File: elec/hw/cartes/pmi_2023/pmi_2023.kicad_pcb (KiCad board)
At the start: 2 copper layers, 149.5 x 73 mm, 298 parts, among them J1 con_servo, J10 Conn_01x01_Pin, J11 Conn_01x01_Socket, J12 Conn_01x01_Pin, J13 Conn_01x01_Pin, J14 Conn_01x01_Socket, J15 Conn_01x01_Socket, J16 Conn_01x01_Pin, J17 Conn_01x01_Pin, J19 Conn_01x01_Pin, J2 con_servo, J20 Conn_01x01_Socket, J21 Conn_01x01_Socket, J22 Conn_01x01_Socket, J23 Conn_01x01_Pin, J24 Conn_01x01_Pin, J27 Conn_01x01_Socket, J28 Conn_01x01_Socket, J29 Conn_01x01_Socket, J3 con_servo, J30 Conn_01x01_Socket, J31 Conn_01x01_Pin, J33 Conn_01x01_Socket, J34 Conn_01x01_Socket, J35 Conn_01x01_Pin, J36 Conn_01x01_Socket, J37 Conn_01x01_Pin, J38 Conn_01x01_Socket, J4 con_servo, J41 Conn_01x01_Socket, J42 Conn_01x01_Socket, J43 Conn_01x01_Socket, J44 Conn_01x01_Pin, J45 Conn_01x01_Socket, J46 Conn_01x01_Pin, J5 254, J7 USB4105-GF-A-060, J8 254, J9 Conn_01x01_Socket, Q2 2N7002, Q3 DMP2008UFG-7, SW1 ESE22MH22, SW2 ESE22MH24, SW3 MSS12C02LS-BB2.0, SW4 2425755-1, SW5 DS1040-04RN, SW7 MSS12C02LS-BB2.0, SW8 MSS12C02LS-BB2.0, U1 DRV8231ADDAR, U10 tof_sensor_master, U11 XRA1200PIG16TR-F, U12 LSM6DSO32XTR, U13 GP2S60B, U14 GP2S60B, U15 GP2S60B, U16 GP2S60B, U18 EESX1321, U19 GP2S60B, U2 DRV8231ADDAR, U20 GP2S60B, U22 VL53L5CXV0GC, U23 PCA9685PW, U24 SN74LVC1T45DBV, U25 SN74LVC1T45DBV, U26 SN74LVC1T45DBV, U27 SN74LVC1T45DBV, U28 TLV61070A, U29 TLV61070A, U3 EESX1321, U30 VL53L5CXV0GC, U32 ESP32-S3-WROOM-1, U33 TLV61070A, U34 TLV61070A, U35 LDL1117S33R, U4 EESX1321, U5 AD8531ARTZ, U6 tof_sensor_master, U7 XRA1200PIG16TR-F, U8 GP2S60B, U9 GP2S60B

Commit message: corrected librariesand ongoing routing
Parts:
- moved R32 52.5 mm to (182.6, 141.5)
- moved R33 52.5 mm to (182.6, 140.0)
- moved R44 10.1 mm to (199.7, 137.3), turned to 0 degrees
- moved R80 0.55 mm to (223.3, 115.8)
- moved R81 0.55 mm to (225.8, 115.8)
- turned R119 to 0 degrees
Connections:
- C28 pad 2: GND -> GND_M
- J6 pad 5: (no net) -> /boards interface/com/esp32_dbg_tx_3v3
- R102 pad 2: GND -> GND_M
- R109 pad 2: GND -> GND_M
- R120 pad 2: GND -> GND_M
- R121 pad 2: GND -> GND_M
- R122 pad 2: GND -> GND_M
- R80 pad 2: /boards interface/interface/esp32_scl_3v3 -> /boards interface/com/scl_3v3
- R81 pad 2: /boards interface/interface/esp32_sda_3v3 -> /boards interface/com/sda_3v3
- U12 pad 12: /boards interface/Sensor module/gyro_mosi_3v3 -> /boards interface/Sensor module/gyro_ncs_3v3
- U12 pad 14: (no net) -> /boards interface/Sensor module/gyro_mosi_3v3
- U31 pad 1: (no net) -> GND_M
- U31 pad 3: /boards interface/interface/esp32_scl_3v3 -> /boards interface/com/scl_3v3
- U31 pad 4: /boards interface/interface/esp32_sda_3v3 -> /boards interface/com/sda_3v3
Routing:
- net GND_M: track 1.33 -> 176.8 mm, vias 0 -> 7
- net +3V3_m: track 0.00 -> 120.3 mm, vias 0 -> 8
- net /boards interface/com/esp32_dbg_rx_3v3: track 0.00 -> 75.1 mm, vias 0 -> 3
- net Net-(U32-TXD0,U0TXD,GPIO43,CLK_OUT1): track 0.00 -> 72.1 mm, vias 0 -> 1
- net /boards interface/com/start_robot_3v3: track 0.00 -> 53.5 mm, vias 0 -> 2
- net /boards interface/Sensor module/gyro_ncs_3v3: track 0.00 -> 37.6 mm, vias 0 -> 1
- net /boards interface/com/left_encod_A_3v3: track 0.00 -> 31.5 mm, vias 0 -> 1
- net /boards interface/Sensor module/gyro_irq_3v3: track 0.00 -> 31.2 mm, vias 0 -> 1
- net /boards interface/Sensor module/gyro_sck_3v3: track 0.00 -> 30.4 mm, vias 0 -> 1
- net /boards interface/Sensor module/gyro_mosi_3v3: track 0.00 -> 30.0 mm, vias 0 -> 1
- net /boards interface/Sensor module/gyro_miso_3v3: track 0.00 -> 29.7 mm, vias 0 -> 1
- net /boards interface/com/left_encod_B_3v3: track 0.00 -> 27.3 mm, vias 0 -> 1
- net /boards interface/com/right_encod_A_3v3: track 0.00 -> 27.2 mm, vias 0 -> 1
- net /boards interface/com/right_encod_B_3v3: track 0.00 -> 25.6 mm, vias 0 -> 1
- net /boards interface/com/led_esp_3v3: track 0.00 -> 21.5 mm, vias 0 -> 1
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
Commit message: wip
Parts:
- removed J10, J12, J13, J16, J17, J19, J23, J24, J31, J35, J37, J44, J46: Conn_01x01_Pin, cocotter_others:board_to_module_small
- removed J11, J14, J15, J20, J21, J22, J27, J28, J29, J30, J33, J34, J36, J38, J41, J42, J43, J45, J9: Conn_01x01_Socket, cocotter_others:board_to_module_small
- removed the R32 at (182.6, 141.5)
- removed the R33 at (182.6, 140.0)
- added J49: ~, pmi_2023_specific:pmi_2023_interconnection, F.Cu at (222.0, 146.4)
- added J50: ~, pmi_2023_specific:pmi_2023_interconnection, F.Cu at (142.5, 145.0)
- U5: footprint cocotter_ic:SOT-23-5 -> cocotter_ic:SOT23-5
- moved R100 43.0 mm to (227.0, 133.0), turned to 0 degrees
- moved R97 40.6 mm to (227.0, 134.5), turned to 0 degrees
- moved R98 40.0 mm to (224.0, 134.5)
- moved R99 40.0 mm to (224.0, 133.0)
- moved R32 14.5 mm to (169.7, 144.4), turned to 180 degrees
- moved R33 14.2 mm to (115.3, 144.5), turned to 0 degrees
- moved R88 8.79 mm to (199.5, 115.0), turned to 90 degrees
- moved R93 8.54 mm to (198.0, 115.0), turned to 90 degrees
- moved D5 2.70 mm to (231.9, 97.8)
- moved R89 2.15 mm to (199.8, 105.9), turned to 90 degrees
- moved D4 1.80 mm to (235.1, 97.8)
- moved R83 1.15 mm to (230.4, 96.2), turned to 0 degrees
- moved R123 0.90 mm to (226.9, 105.3)
- moved R128 0.60 mm to (218.5, 106.1)
- moved R82 0.32 mm to (233.5, 96.2), turned to 0 degrees
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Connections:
- C51 pad 2: GND -> GND_M
- C52 pad 2: GND -> GND_M
- C53 pad 2: GND -> GND_M
- C57 pad 2: GND -> GND_M
- C58 pad 2: GND -> GND_M
- C59 pad 2: GND -> GND_M
- R100 pad 2: /boards interface/com/scl_3v3 -> /boards interface/sda_top_3v3
- R115 pad 2: /boards interface/com/i2C_io_int_3v3 -> /boards interface/i2c_io_int_3v3
- R123 pad 2: /boards interface/Sensor module/tof_irq_3v3 -> /boards interface/tof_irq_3v3
- R124 pad 2: GND -> GND_M
- R127 pad 2: GND -> GND_M
- R128 pad 2: GND -> GND_M
- R131 pad 2: GND -> GND_M
- R33 pad 2: /sensors/ctc_rigth -> /sensors/ctc_right
- R65 pad 2: /power_supply/vbatt_mon_4.35V -> /boards interface/vbatt_mon_4.35V
- R80 pad 2: /boards interface/com/scl_3v3 -> /boards interface/scl_top_3v3
- R81 pad 2: /boards interface/com/sda_3v3 -> /boards interface/sda_top_3v3
- R97 pad 2: /boards interface/com/sda_3v3 -> /boards interface/scl_top_3v3
- SW2 pad 1: /sensors/ctc_rigth -> /sensors/ctc_right
- U10 pad 4: unconnected-(U10-detect_irq_3v3-Pad4) -> /sensors/tof_irq
- U11 pad 13: /boards interface/com/i2C_io_int_3v3 -> /boards interface/i2c_io_int_3v3
- U11 pad 14: /boards interface/com/scl_3v3 -> /boards interface/scl_top_3v3
- U11 pad 15: /boards interface/com/sda_3v3 -> /boards interface/sda_top_3v3
- U11 pad 7: /boards interface/interface/select2 -> /boards interface/interface/select4
- U11 pad 9: /boards interface/interface/conf3 -> /boards interface/interface/select2
- U22 pad A2: GND -> GND_M
- U22 pad A3: /boards interface/Sensor module/tof_irq_3v3 -> /boards interface/tof_irq_3v3
- U22 pad A6: GND -> GND_M
- U22 pad A7: GND -> GND_M
- U22 pad B4: GND -> GND_M
- U22 pad C1: GND -> GND_M
- U22 pad C3: /boards interface/Sensor module/SDA_3v3 -> /boards interface/sda_top_3v3
- U22 pad C4: /boards interface/Sensor module/SCL_3V3 -> /boards interface/scl_top_3v3
- U22 pad C6: GND -> GND_M
- U22 pad C7: GND -> GND_M
- U30 pad A2: GND -> GND_M
- U30 pad A3: /boards interface/Sensor module/tof_irq_3v3 -> /boards interface/tof_irq_3v3
- U30 pad A6: GND -> GND_M
- U30 pad A7: GND -> GND_M
- U30 pad B4: GND -> GND_M
- U30 pad C1: GND -> GND_M
- U30 pad C3: /boards interface/Sensor module/SDA_3v3 -> /boards interface/sda_top_3v3
- U30 pad C4: /boards interface/Sensor module/SCL_3V3 -> /boards interface/scl_top_3v3
- U30 pad C6: GND -> GND_M
- U30 pad C7: GND -> GND_M
- U31 pad 3: /boards interface/com/scl_3v3 -> /boards interface/scl_top_3v3
- U31 pad 4: /boards interface/com/sda_3v3 -> /boards interface/sda_top_3v3
- U32 pad 10: /boards interface/com/CAN_tx_3v3 -> /boards interface/scl_top_3v3
- U32 pad 11: /boards interface/com/CAN_rx_3v3 -> /boards interface/sda_top_3v3
- U32 pad 12: /boards interface/com/pwm_right -> /boards interface/tof_irq_3v3
- U32 pad 15: /boards interface/com/i_prop_right_3v3 -> unconnected-(U32-IO3,RTC_GPIO3,GPIO3,TOUCH3,ADC1_CH2-Pad15)
- U32 pad 17: /boards interface/com/dir_right -> /boards interface/com/i_prop_right_3v3
- U32 pad 18: /boards interface/Sensor module/gyro_ncs_3v3 -> /boards interface/com/i_prop_left_3v3
- U32 pad 19: /boards interface/Sensor module/gyro_mosi_3v3 -> /boards interface/i2c_io_int_3v3
- U32 pad 20: /boards interface/Sensor module/gyro_sck_3v3 -> /boards interface/com/dir_right
- U32 pad 21: /boards interface/Sensor module/gyro_miso_3v3 -> /boards interface/com/pwm_right
- U32 pad 22: /boards interface/Sensor module/gyro_irq_3v3 -> /boards interface/com/dir_left
- U32 pad 23: /boards interface/com/emergency_stop_3v3 -> /boards interface/com/pwm_left
- U32 pad 24: /boards interface/com/tof_irq -> /boards interface/com/ctc_right
- U32 pad 25: /boards interface/com/i2C_io_int_3v3 -> /boards interface/Sensor module/gyro_sck_3v3
- U32 pad 28: /boards interface/com/start_robot_3v3 -> /boards interface/Sensor module/gyro_miso_3v3
- U32 pad 29: /boards interface/com/sda_3v3 -> /boards interface/Sensor module/gyro_mosi_3v3
- U32 pad 30: /boards interface/com/scl_3v3 -> /boards interface/Sensor module/gyro_ncs_3v3
- U32 pad 31: unconnected-(U32-IO38,GPIO38,FSPIWP,SUBSPIWP-Pad31) -> /boards interface/Sensor module/gyro_irq_3v3
- U32 pad 32: /boards interface/com/right_encod_B_3v3 -> /boards interface/com/left_encod_A_3v3
- U32 pad 33: /boards interface/com/right_encod_A_3v3 -> /boards interface/com/left_encod_B_3v3
- U32 pad 34: /boards interface/com/left_encod_B_3v3 -> /boards interface/com/right_encod_B_3v3
- U32 pad 35: /boards interface/com/left_encod_A_3v3 -> /boards interface/com/right_encod_A_3v3
- U32 pad 38: /boards interface/com/i_prop_left_3v3 -> /boards interface/com/start_robot_3v3
- U32 pad 6: /boards interface/com/pwm_left -> /boards interface/com/ctc_left
- U32 pad 7: /boards interface/com/dir_left -> /boards interface/interface/conf3
- U32 pad 8: /boards interface/com/ctc_right -> /boards interface/com/emergency_stop_3v3
- U32 pad 9: /boards interface/com/ctc_left -> /boards interface/Sensor module/enable_front_tof_3v3
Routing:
- net GND_M: track 176.8 -> 581.8 mm, vias 7 -> 100
- net +3V3_m: track 120.3 -> 309.7 mm, vias 8 -> 20
- net /boards interface/sda_top_3v3: track 0.00 -> 96.0 mm, vias 0 -> 6
- net /boards interface/tof_irq_3v3: track 0.00 -> 91.2 mm, vias 0 -> 7
- net /boards interface/com/ctc_left: track 1.90 -> 90.5 mm, vias 1 -> 0
- net /boards interface/scl_top_3v3: track 0.00 -> 87.4 mm, vias 0 -> 5
- net /boards interface/i2c_io_int_3v3: track 0.00 -> 62.4 mm, vias 0 -> 5
- net /boards interface/vbatt_mon_4.35V: track 0.00 -> 59.6 mm, vias 0 -> 3
- net /boards interface/com/vbatt_mon_4.35V: track 1.50 -> 60.7 mm, vias 0 -> 1
- net /power_supply/vbatt_mon_4.35V: track 52.9 -> 0.00 mm, vias 3 -> 0
- net /boards interface/com/pwm_right: track 0.00 -> 48.2 mm, vias 0 -> 2
- net /boards interface/com/dir_right: track 1.82 -> 48.0 mm, vias 1 -> 2
- net /boards interface/com/right_encod_A_3v3: track 27.2 -> 72.0 mm, vias 1 -> 2
- net /boards interface/com/i_prop_right_3v3: track 1.90 -> 46.7 mm, vias 1 -> 0
- net /boards interface/com/pwm_left: track 1.91 -> 44.4 mm, vias 1 -> 0
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- added copper zone on B.Cu, net GND_M
- added copper zone on F.Cu, net GND_M
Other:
- outline, holes or cut-outs redrawn

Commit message: wip
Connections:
- R75 pad 2: Net-(D1-C_BLUE) -> Net-(D1-C_GREEN)
- R76 pad 2: Net-(D1-C_GREEN) -> Net-(D1-C_BLUE)
- U23 pad 20: /actuators/led_RGB_g_3v3 -> /actuators/led_RGB_b_3v3
- U23 pad 21: /actuators/led_RGB_b_3v3 -> /actuators/led_RGB_g_3v3
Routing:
- net (no net): track 137.9 -> 0.00 mm, vias 10 -> 0
- net /actuators/led_RGB_g_3v3: track 0.00 -> 73.1 mm, vias 0 -> 6
- net /actuators/led_RGB_b_3v3: track 0.00 -> 63.9 mm, vias 0 -> 4
- net +3V3_m: track 309.7 -> 315.6 mm
- net /actuators/sda_3v3: track 198.7 -> 196.3 mm
- net Net-(D1-C_BLUE): track 0.00 -> 2.34 mm
- net /actuators/scl_3v3: track 196.2 -> 194.3 mm
- net /sensors/line_led_3v3: track 62.9 -> 61.3 mm
- net /actuators/led_RGB_r_3v3: track 67.1 -> 65.7 mm
- net +BATT: track 146.2 -> 145.2 mm
- net /power_supply/Vmot_right_5V: track 69.8 -> 68.8 mm
- net /propulsion/encoder_supply: track 64.8 -> 63.9 mm
- net Net-(D1-C_GREEN): track 1.35 -> 2.26 mm
- net /boards interface/sda_top_3v3: track 96.0 -> 95.1 mm
- net /actuators/enable_tof_3v3: track 145.8 -> 145.1 mm
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
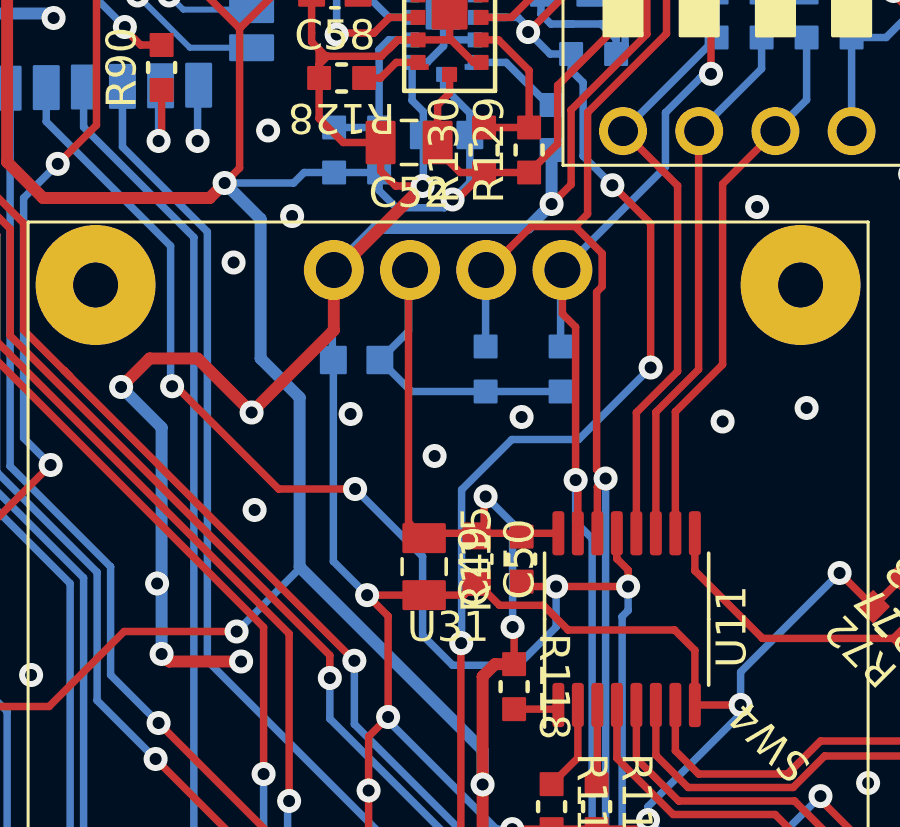
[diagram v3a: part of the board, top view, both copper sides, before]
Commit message: added oled display power supply res selectors, jlcpcb refs : wip
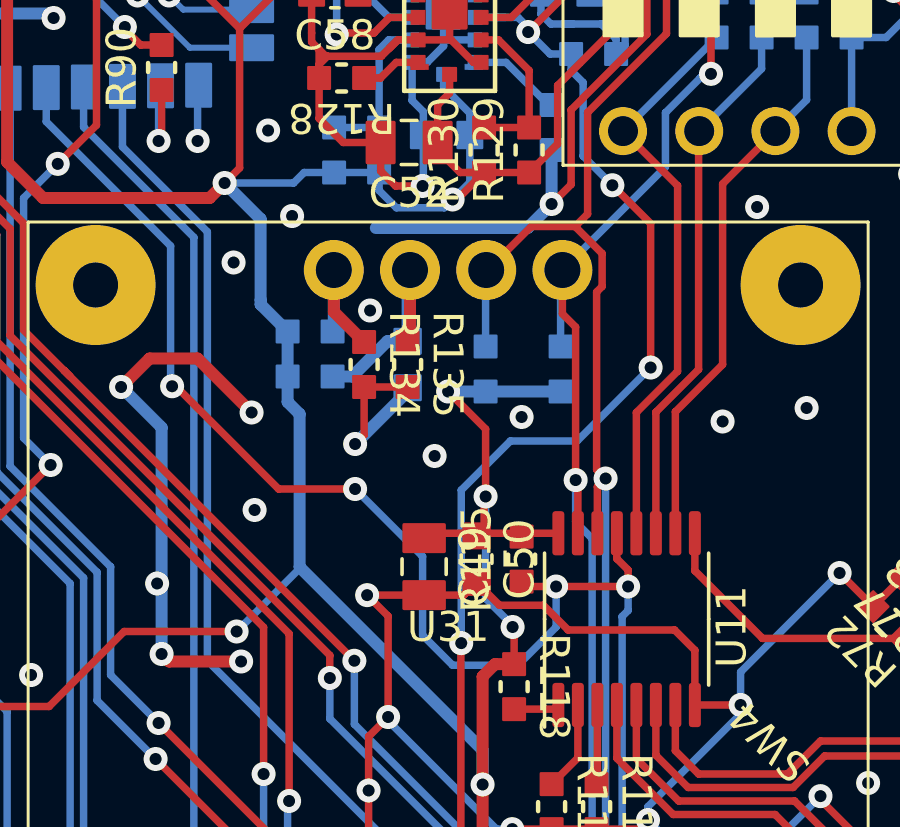
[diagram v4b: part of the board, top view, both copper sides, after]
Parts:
- added R132: 0R, cocotter_resistor:r0603_reflow, B.Cu at (217.4, 116.0)
- added R133: 0R, cocotter_resistor:r0603_reflow, B.Cu at (217.4, 114.5)
- added R134: 0R, cocotter_resistor:r0603_reflow, F.Cu at (219.2, 115.7)
- added R135: 0R, cocotter_resistor:r0603_reflow, F.Cu at (220.7, 115.7)
- moved C31 1.71 mm to (220.7, 115.7), turned to -90 degrees
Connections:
- C31 pad 1: +3V3_m -> Net-(U31-VCC)
- U31 pad 1: GND_M -> Net-(U31-GND)
- U31 pad 2: +3V3_m -> Net-(U31-VCC)
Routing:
- net GND_M: track 582.5 -> 565.3 mm, vias 110 -> 111
- net +3V3_m: track 315.6 -> 304.6 mm, vias 20 -> 21
- net Net-(U31-VCC): track 0.00 -> 7.83 mm
- net Net-(U31-GND): track 0.00 -> 5.04 mm

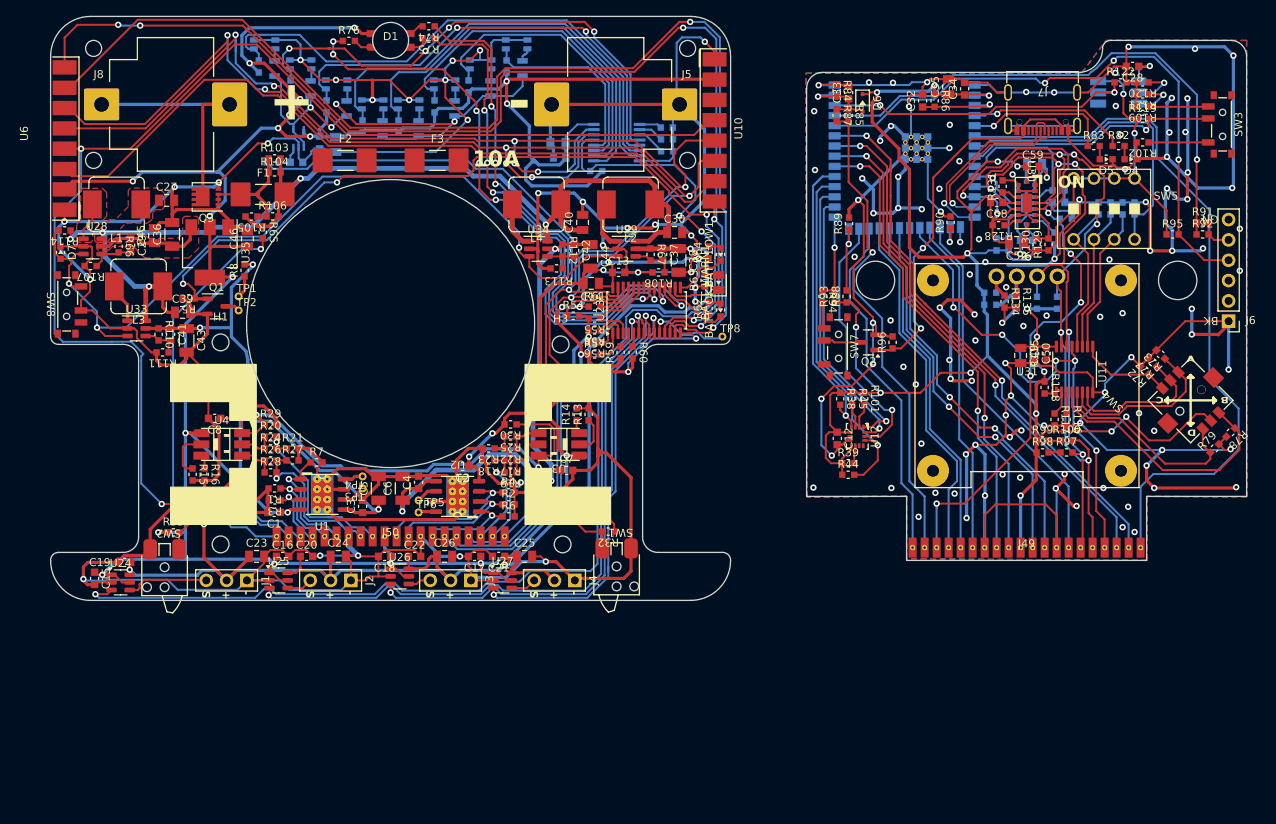
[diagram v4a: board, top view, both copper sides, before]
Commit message: 3d models added
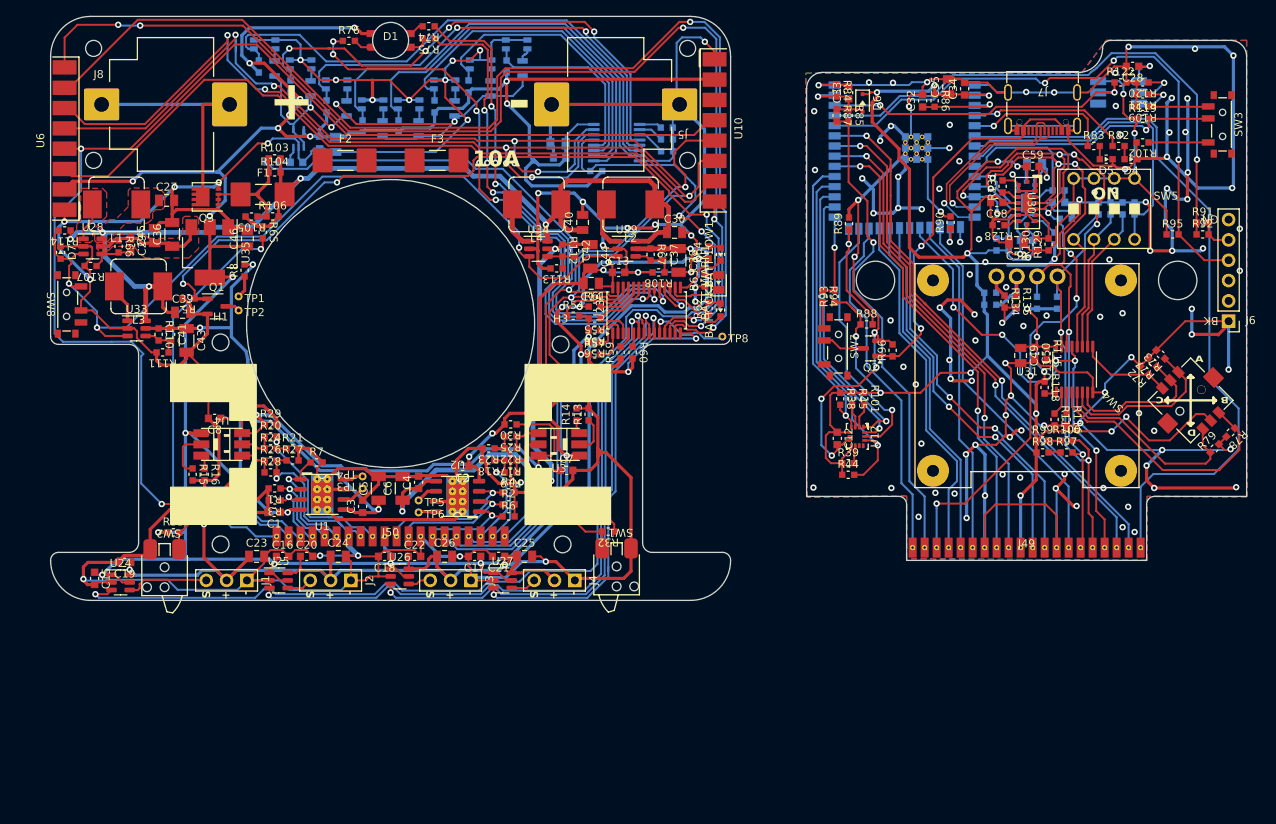
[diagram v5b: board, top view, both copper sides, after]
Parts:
- BATT_LOW1, BATT_OK1, D4, D5, D7: footprint cocotter_diodes:LED_0603_1608Metric -> lib_export:LED_0603_1608Metric
- BATT_WARN1: footprint cocotter_diodes:LED_0805_2012Metric -> lib_export:LED_0805_2012Metric
- C1, C10, C12, C13, C15, C16, C17, C18, C19, C2, C20, C21, C22, C28, C29, C3, C31, C32, C33, C34, C37, C4, C41, C42, C47, C50, C53, C57, C58, C59, C7, C8, C9: footprint cocotter_capacitors:C_0603_1608Metric -> lib_export:C_0603_1608Metric
- C11, C14, C23, C24, C25, C26, C27, C30, C35, C39, C40, C45, C46, C48, C49, C51, C52: footprint cocotter_capacitors:C_0805_2012Metric -> lib_export:C_0805_2012Metric
- C36, C38, C43, C44, C5, C6: footprint cocotter_capacitors:C_1206_3216Metric -> lib_export:C_1206_3216Metric
- D6: footprint cocotter_diodes:D_SOD-323F -> lib_export:D_SOD-323F
- F1, F2, F3: footprint cocotter_others:JFC2410 -> lib_export:JFC2410
- H1, H2, H3, H4: footprint MountingHole:MountingHole_2.1mm -> lib_export:MountingHole_2.1mm
- J49, J50: footprint pmi_2023_specific:pmi_2023_interconnection -> lib_export:pmi_2023_interconnection
- J5, J8: footprint cocotter_connectors:MY-18650-02 -> lib_export:MY-18650-02
- J6: footprint cocotter_connectors:TTL-232R-3V3 -> lib_export:TTL-232R-3V3
- J7: footprint cocotter_connectors:USB4105 -> lib_export:USB4105
- Q2: footprint Package_TO_SOT_SMD:SOT-23 -> lib_export:SOT-23
- Q3: footprint cocotter_transistors:Diodes_PowerDI3333-8 -> lib_export:Diodes_PowerDI3333-8
- SW1: footprint cocotter_connectors:ESE22MH22 -> lib_export:ESE22MH22
- SW2: footprint cocotter_connectors:ESE22MH24 -> lib_export:ESE22MH24
- TP1, TP2, TP3, TP4, TP5, TP6, TP8: footprint cocotter_others:testpoint-THT-0.5mm -> lib_export:testpoint-THT-0.5mm
- U10, U6: footprint cocotter_connectors:tof_sensor_male -> lib_export:tof_sensor_male
- U11, U7: footprint cocotter_ic:TSSOP-16_4.4x5mm_P0.65mm -> lib_export:TSSOP-16_4.4x5mm_P0.65mm
- U12: footprint cocotter_ic:LGA-14_3x2.5mm_P0.5mm_LayoutBorder3x4y -> lib_export:LGA-14_3x2.5mm_P0.5mm_LayoutBorder3x4y
- U23: footprint Package_SO:TSSOP-28_4.4x9.7mm_P0.65mm -> lib_export:TSSOP-28_4.4x9.7mm_P0.65mm
- U24, U25, U26, U27: footprint Package_TO_SOT_SMD:SOT-23-6 -> lib_export:SOT-23-6
- U28, U29, U33, U34: footprint cocotter_ic:SOT-23-6 -> lib_export:SOT-23-6
- U35: footprint cocotter_ic:SOT-223 -> lib_export:SOT-223
- U5: footprint cocotter_ic:SOT23-5 -> lib_export:SOT23-5
- moved R88 4.30 mm to (202.0, 118.5), turned to 0 degrees
- moved R96 1.00 mm to (205.2, 121.8)
- moved Q2 0.79 mm to (202.5, 121.5)
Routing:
- net Net-(U32-IO45,GPIO45): track 9.61 -> 15.2 mm
- net Net-(Q2-D): track 4.72 -> 5.28 mm
- net GND_M: track 565.3 -> 565.6 mm, vias 111 -> 113
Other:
- outline, holes or cut-outs redrawn

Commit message: 3d models updated: wip
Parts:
- F1, F2, F3: footprint lib_export:JFC2410 -> cocotter_others:JFC2410
- Q3: footprint lib_export:Diodes_PowerDI3333-8 -> cocotter_transistors:Diodes_PowerDI3333-8
- SW1: footprint lib_export:ESE22MH22 -> cocotter_connectors:ESE22MH22
- SW2: footprint lib_export:ESE22MH24 -> cocotter_connectors:ESE22MH24
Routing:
- added copper zone on F.Cu, net Net-(Q3-D)
